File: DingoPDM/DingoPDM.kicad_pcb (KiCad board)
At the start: 4 copper layers, 72.4 x 95.2 mm, 155 parts, among them J1 RedCubeTerminal, J2 RedCubeTerminal, J3 Conn_01x12, J4 TC, J5 USB_C_Receptacle_USB2.0, SW1 BOOT, U1 VXO7805-500-M, U10 BTS7008-2EPA, U11 BTS7008-2EPA, U12 LM324, U13 BTS7008-2EPA, U14 OKI-78SR-5_1.5-W36H-C, U15 TSR_1-2450, U2 LD1117S33CTR, U3 PCA82C250, U4 STM32F446RETx, U5 MB85RC256V, U6 MCP9808, U7 LM324, U8 BTS700n-1EPP, U9 BTS700n-1EPP, Y1 8mHz

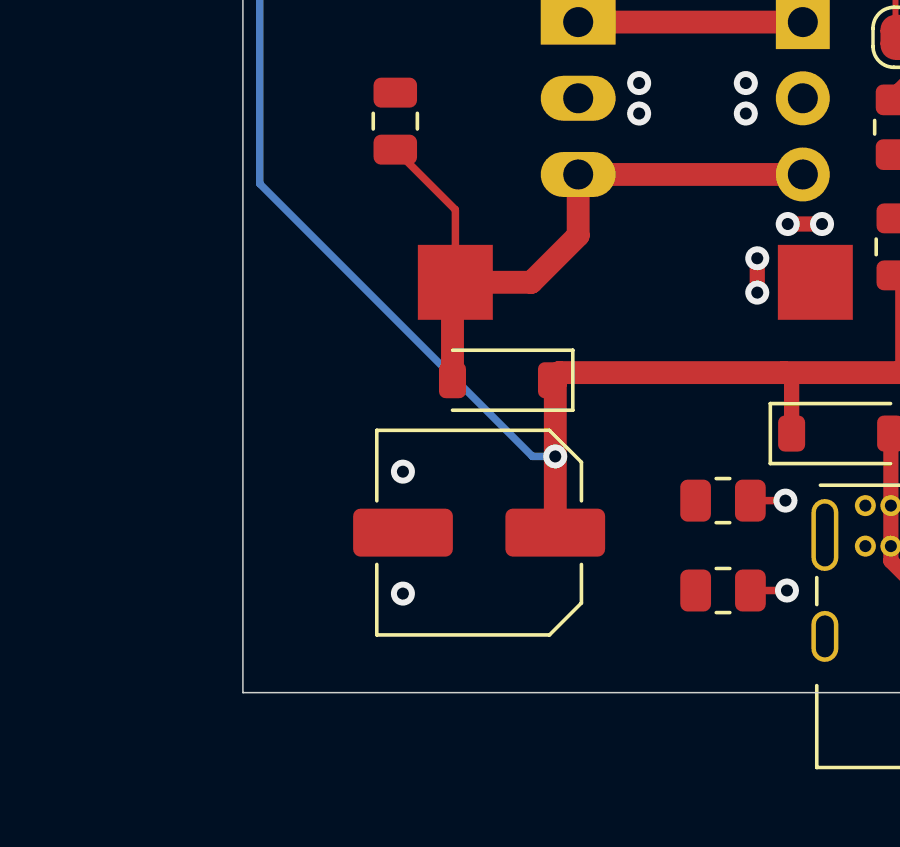
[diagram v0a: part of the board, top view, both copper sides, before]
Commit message: switch to ceramic caps
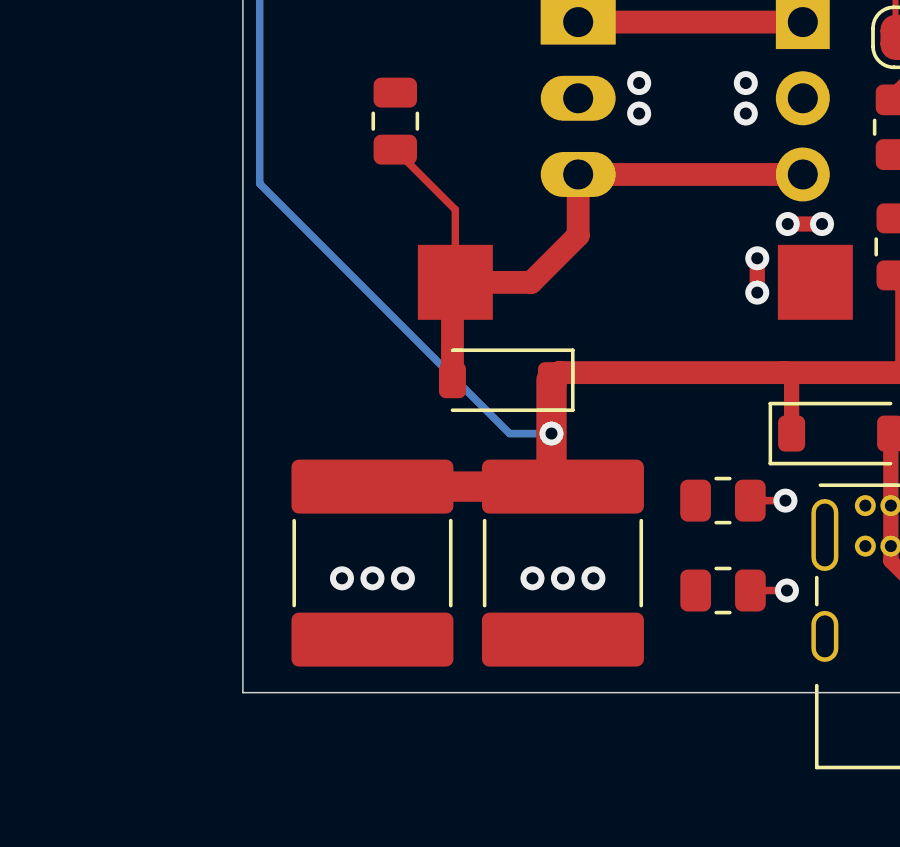
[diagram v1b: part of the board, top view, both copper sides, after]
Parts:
- added C42: 100uF, Capacitor_SMD:C_2220_5750Metric, F.Cu at (-27.2, 57.7)
- C41: footprint Capacitor_SMD:C_Elec_6.3x7.7 -> Capacitor_SMD:C_2220_5750Metric
- moved C41 3.70 mm to (-33.5, 57.7), turned to -90 degrees
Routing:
- net +5V: track 147.2 -> 151.8 mm
- net GND: vias 67 -> 71

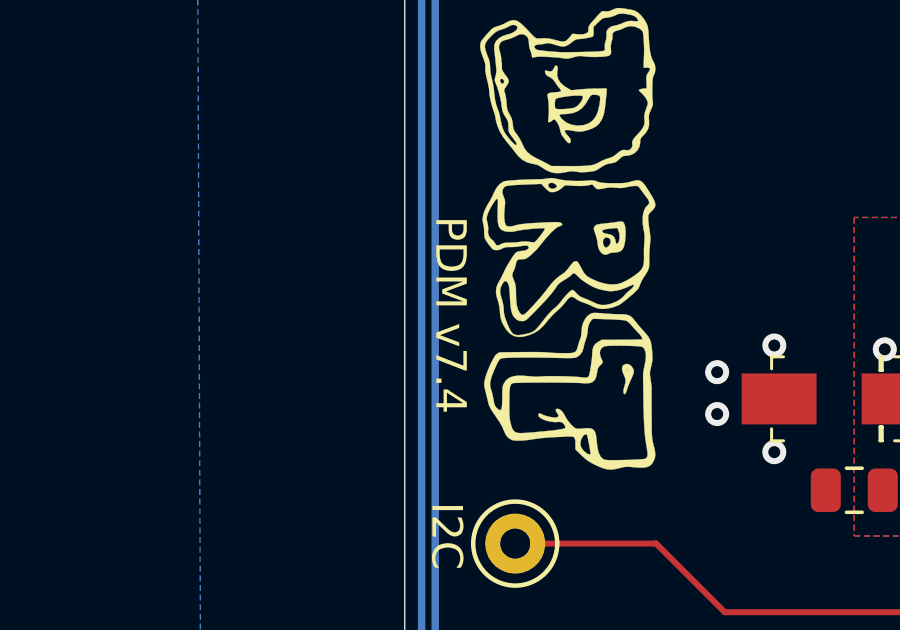
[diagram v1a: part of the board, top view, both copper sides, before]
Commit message: updated silk version
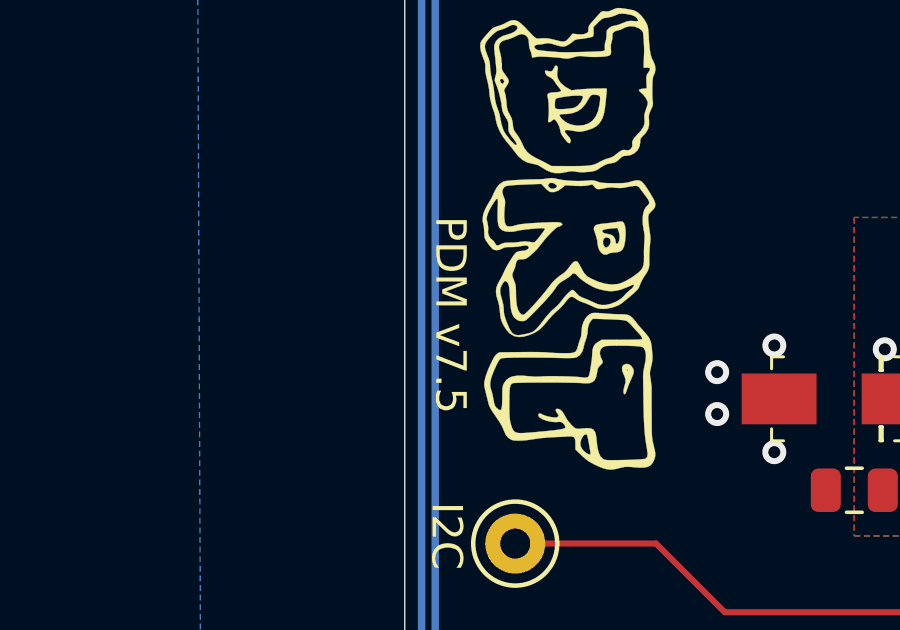
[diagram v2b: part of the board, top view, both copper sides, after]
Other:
- board text added: "PDM v7.5"
- board text removed: "PDM v7.4"
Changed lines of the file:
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@@
 		)
 	)
-	(gr_text "PDM v7.4"
+	(gr_text "PDM v7.5"
 		(at -36.322 3.302 270)
 		(layer "F.SilkS")

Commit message: move footprints to project library
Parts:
- C41, C42: value 100uF -> 47uF
- D10, D8: footprint digikey-footprints:DO-214AC -> dingoPDM:DO-214AC
- D2: footprint digikey-footprints:DO-214AB_TVS -> dingoPDM:DO-214AB_TVS
- D4: footprint digikey-footprints:SOT-23-3 -> dingoPDM:SOT-23-3
- G1: footprint DRTLogo:DRTLogo -> dingoPDM:DRTLogo
- G2: footprint DRTLogo:DingoFaceNoFill -> dingoPDM:DingoFaceNoFill
- J1, J2: footprint RedCube:M6_Hole_8Pin_7461084 -> dingoPDM:M6_Hole_8Pin_7461084
- J3: footprint Deutsch_DT:DT15-12PA -> dingoPDM:DT15-12PA
- SW1: footprint SlideSwitch:CJS-1200TB -> dingoPDM:CJS-1200TB
- U1: footprint CUI_Regulators:VXO78x-500-M -> dingoPDM:VXO78x-500-M
- U10, U11, U13, U8, U9: footprint Profet:TDSO-14 -> dingoPDM:TDSO-14
- U14: footprint Converter_DCDC:Converter_DCDC_Murata_OKI-78SR_Horizontal -> dingoPDM:Converter_DCDC_Murata_OKI-78SR_Horizontal
- U15: footprint Converter_DCDC:Converter_DCDC_TRACO_TSR-1_THT -> dingoPDM:Converter_DCDC_TRACO_TSR-1_THT
- U2: footprint digikey-footprints:SOT-223 -> dingoPDM:SOT-223
- Y1: footprint Crystals_Modify:Crystal_SMD_5032-2Pin_5.0x3.2mm_HandSoldering -> dingoPDM:Crystal_SMD_5032-2Pin_5.0x3.2mm_HandSoldering
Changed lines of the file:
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@@
 		)
 	)
-	(footprint "Crystals_Modify:Crystal_SMD_5032-2Pin_5.0x3.2mm_HandSoldering"
+	(footprint "dingoPDM:Crystal_SMD_5032-2Pin_5.0x3.2mm_HandSoldering"
 		(layer "F.Cu")
 		(at 5.842 55.8546)
@@
 		)
 	)
-	(footprint "RedCube:M6_Hole_8Pin_7461084"
+	(footprint "dingoPDM:M6_Hole_8Pin_7461084"
 		(layer "F.Cu")
 		(at -24.638 27.178)
@@
 		)
 	)
-	(footprint "Profet:TDSO-14"
+	(footprint "dingoPDM:TDSO-14"
 		(layer "F.Cu")
 		(at 11.1448 12.7 90)
@@
 		)
 		(property "Digi-Key_PN" "BTS70021EPPXUMA1CT-ND"
-			(at 23.8448 1.5552 0)
+			(at 1.778 23.622 0)
 			(layer "F.Fab")
 			(hide yes)
@@
 		)
 		(property "LCSC" "C534824"
-			(at 23.8448 1.5552 0)
+			(at 1.778 23.622 0)
 			(layer "F.Fab")
 			(hide yes)
@@
 		)
 	)
-	(footprint "Profet:TDSO-14"
+	(footprint "dingoPDM:TDSO-14"
 		(layer "F.Cu")
 		(at 0.082 12.7 90)
@@
 			)
 		)
-		(property "Digi-Key_PN" "BTS70082EPAXUMA1CT-ND"
-			(at 12.782 12.618 0)
+		(property "Digi-Key_PN" "BTS70021EPPXUMA1CT-ND"
+			(at 1.778 23.622 0)
 			(layer "F.Fab")
 			(hide yes)
@@
 			)
 		)
-		(property "LCSC" "C2150060"
-			(at 12.782 12.618 0)
+		(property "LCSC" "C534824"
+			(at 1.778 23.622 0)
 			(layer "F.Fab")
 			(hide yes)
@@
 		)
 	)
-	(footprint "Deutsch_DT:DT15-12PA"
+	(footprint "dingoPDM:DT15-12PA"
 		(layer "F.Cu")
 		(at 0 0 -90)
@@
 		)
 	)
-	(footprint "CUI_Regulators:VXO78x-500-M"
+	(footprint "dingoPDM:VXO78x-500-M"
 		(layer "F.Cu")
 		(at -24.765 42.799 -90)
@@
 		)
 	)
-	(footprint "digikey-footprints:SOT-23-3"
+	(footprint "dingoPDM:SOT-23-3"
 		(layer "F.Cu")
 		(at -8.8748 -11.2212 -90)
@@
 		)
 	)
-	(footprint "DRTLogo:DRTLogo"
+	(footprint "dingoPDM:DRTLogo"
 		(layer "F.Cu")
 		(at -32.4104 0.762 -90)
@@
 		)
 	)
-	(footprint "digikey-footprints:DO-214AC"
+	(footprint "dingoPDM:DO-214AC"
 		(layer "F.Cu")
 		(at -23.368 6.096 180)
@@
 		)
 	)
-	(footprint "Profet:TDSO-14"
+	(footprint "dingoPDM:TDSO-14"
 		(layer "F.Cu")
 		(at 8.9604 -12.5528 -90)
 		(descr "Original name <b>SOP65P600X115-15N-V</b><p>Max Component Height - 1.15mm")
 		(property "Reference" "U10"
-			(at 0.73 -4.07 90)
+			(at 0.73 -4.07 270)
 			(layer "F.SilkS")
 			(hide yes)
@@
 		)
 		(property "Value" "BTS7008-2EPA"
-			(at 14.974 4.124 90)
+			(at 14.974 4.124 270)
 			(layer "F.Fab")
 			(hide yes)
@@
 			)
 		)
-		(property "Digi-Key_PN" "BTS70082EPAXUMA1CT-ND"
-			(at 21.5132 -3.5924 0)
+		(property "Digi-Key_PN" "BTS70021EPPXUMA1CT-ND"
+			(at 1.778 23.622 180)
 			(layer "F.Fab")
 			(hide yes)
@@
 			)
 		)
-		(property "LCSC" "C2150060"
-			(at 21.5132 -3.5924 0)
+		(property "LCSC" "C534824"
+			(at 1.778 23.622 180)
 			(layer "F.Fab")
 			(hide yes)
@@
 		)
 	)
-	(footprint "Profet:TDSO-14"
+	(footprint "dingoPDM:TDSO-14"
 		(layer "F.Cu")
 		(at 0.0104 -12.6544 -90)
 		(descr "Original name <b>SOP65P600X115-15N-V</b><p>Max Component Height - 1.15mm")
 		(property "Reference" "U13"
-			(at 0.73 -4.07 90)
+			(at 0.73 -4.07 270)
 			(layer "F.SilkS")
 			(hide yes)
@@
 		)
 		(property "Value" "BTS7008-2EPA"
-			(at 14.974 4.124 90)
+			(at 14.974 4.124 270)
 			(layer "F.Fab")
 			(hide yes)
@@
 			)
 		)
-		(property "Digi-Key_PN" "BTS70082EPAXUMA1CT-ND"
-			(at 12.6648 -12.644 0)
+		(property "Digi-Key_PN" "BTS70021EPPXUMA1CT-ND"
+			(at 1.778 23.622 180)
 			(layer "F.Fab")
 			(hide yes)
@@
 			)
 		)
-		(property "LCSC" "C2150060"
-			(at 12.6648 -12.644 0)
+		(property "LCSC" "C534824"
+			(at 1.778 23.622 180)
 			(layer "F.Fab")
 			(hide yes)
@@
 		)
 	)
-	(footprint "Converter_DCDC:Converter_DCDC_TRACO_TSR-1_THT"
+	(footprint "dingoPDM:Converter_DCDC_TRACO_TSR-1_THT"
 		(layer "F.Cu")
 		(at -26.67 39.624 -90)
@@
 		)
 	)
-	(footprint "digikey-footprints:DO-214AC"
+	(footprint "dingoPDM:DO-214AC"
 		(layer "F.Cu")
 		(at 22.86 6.096)
 		(property "Reference" "D8"
-			(at 0 -2.6 0)
+			(at 0 -2.6 180)
 			(layer "F.SilkS")
 			(hide yes)
@@
 		)
 		(property "Value" "BYG23M"
-			(at 0 2.45 0)
+			(at 0 2.45 180)
 			(layer "F.Fab")
 			(hide yes)
@@
 		)
 		(property "Digi-Key_PN" "BYG23M-E3/TR3GICT-ND"
-			(at 0 0 0)
+			(at -46.736 12.192 180)
 			(layer "F.Fab")
 			(hide yes)
@@
 		)
 		(property "LCSC" "C141573"
-			(at 0 0 0)
+			(at -46.736 12.192 180)
 			(layer "F.Fab")
 			(hide yes)
@@
 		)
 	)
-	(footprint "digikey-footprints:SOT-223"
+	(footprint "dingoPDM:SOT-223"
 		(layer "F.Cu")
 		(at -11.3386 44.094)
@@
 		)
 	)
-	(footprint "Converter_DCDC:Converter_DCDC_Murata_OKI-78SR_Horizontal"
+	(footprint "dingoPDM:Converter_DCDC_Murata_OKI-78SR_Horizontal"
 		(layer "F.Cu")
 		(at -19.182 39.624 -90)
@@
 		(embedded_fonts no)
 	)
-	(footprint "Profet:TDSO-14"
+	(footprint "dingoPDM:TDSO-14"
 		(layer "F.Cu")
 		(at -10.922 12.7 90)
@@
 		)
 	)
-	(footprint "digikey-footprints:DO-214AB_TVS"
+	(footprint "dingoPDM:DO-214AB_TVS"
 		(layer "F.Cu")
 		(at -33.655 30.586 -90)
@@
 		)
 	)
-	(footprint "SlideSwitch:CJS-1200TB"
+	(footprint "dingoPDM:CJS-1200TB"
 		(layer "F.Cu")
 		(at -5.461 58.166 90)
@@
 			)
 		)
-		(property "Value" "100uF"
+		(property "Value" "47uF"
 			(at 0 3.65 270)
 			(layer "F.Fab")
@@
 			)
 		)
-		(property "Value" "100uF"
+		(property "Value" "47uF"
 			(at 0 3.65 270)
 			(layer "F.Fab")
@@
 		)
 	)
-	(footprint "RedCube:M6_Hole_8Pin_7461084"
+	(footprint "dingoPDM:M6_Hole_8Pin_7461084"
 		(layer "F.Cu")
 		(at -30.48 -27.178)
@@
 		)
 	)
-	(footprint "DRTLogo:DingoFaceNoFill"
+	(footprint "dingoPDM:DingoFaceNoFill"
 		(layer "B.Cu")
 		(at -25.781 -7.493 180)
@@
 		)
 		(property "Datasheet" ""
-			(at 0 0 180)
+			(at 0 0 0)
 			(layer "F.Fab")
 			(hide yes)
@@
 		)
 		(property "Description" ""
-			(at 0 0 180)
+			(at 0 0 0)
 			(layer "F.Fab")
 			(hide yes)

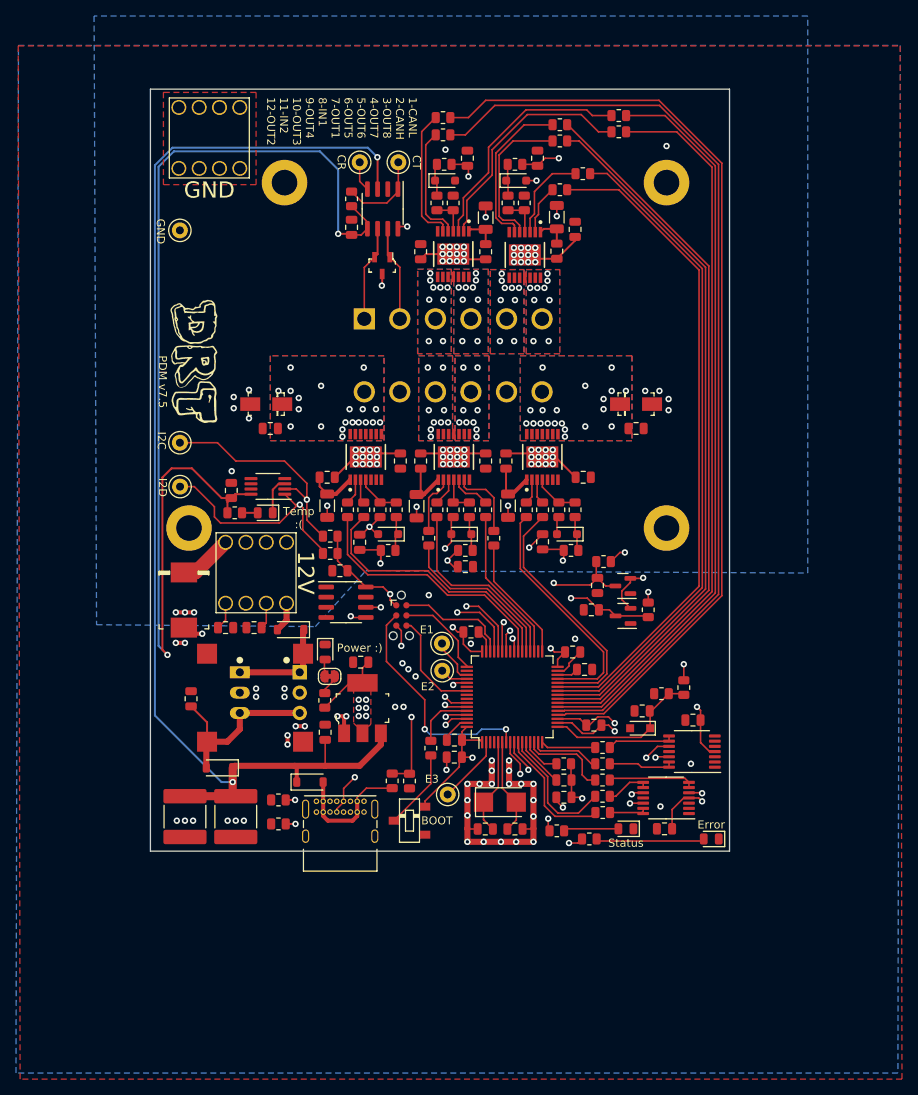
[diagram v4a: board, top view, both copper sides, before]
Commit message: make v7.6 changes, update can transceiver
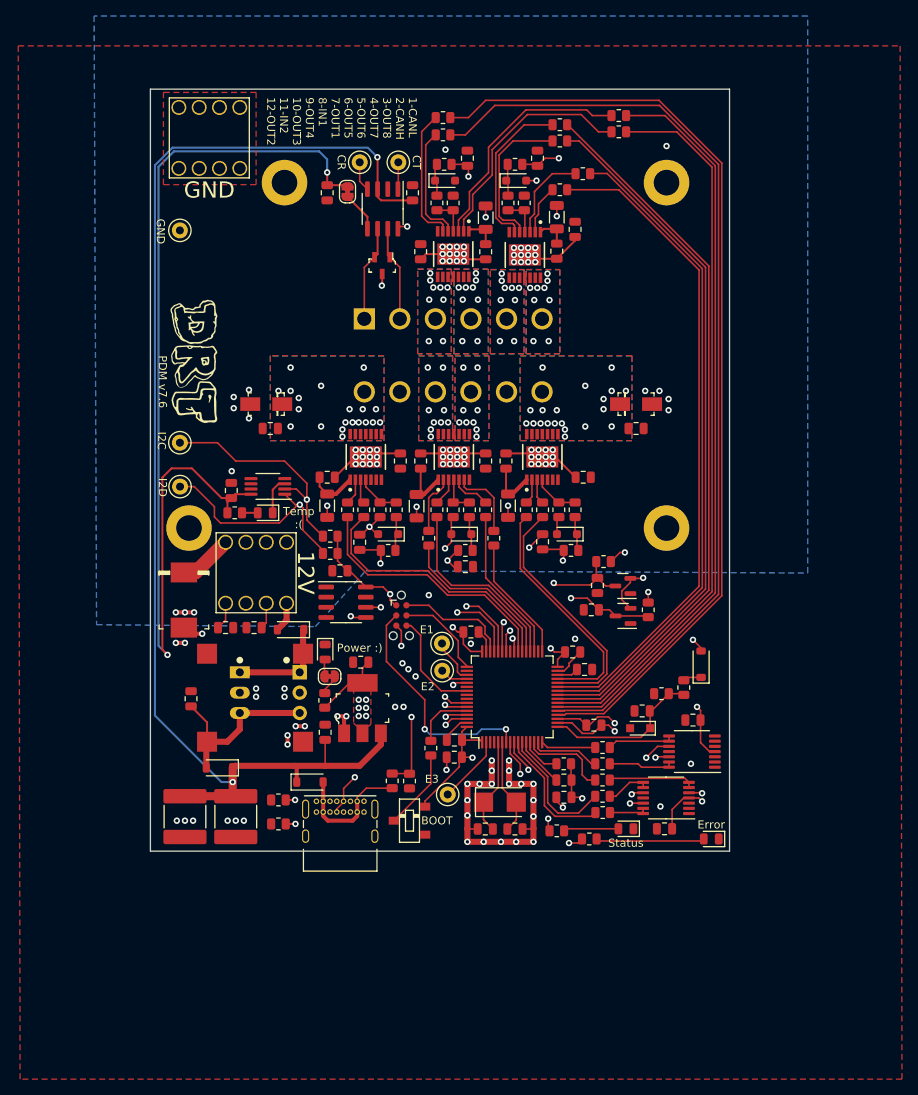
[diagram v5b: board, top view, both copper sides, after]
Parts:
- removed R5: 1K, Resistor_SMD:R_0805_2012Metric
- added C43: 100nF, Capacitor_SMD:C_0805_2012Metric, F.Cu at (-5.08, -20.3)
- added D20: Schottky, Diode_SMD:D_SOD-123, F.Cu at (31.0, 38.6)
- added JP2: VioJumper, Jumper:SolderJumper-2_P1.3mm_Bridged_RoundedPad1.0x1.5mm, F.Cu at (-13.2, -20.5)
- U3: value PCA82C250 -> TJA1042T/3
- moved C9 5.29 mm to (-15.7, -20.3), turned to -90 degrees
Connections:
- R1 pad 1: +12V -> Net-(D20-K)
- U3 pad 5: +3V3 -> Net-(JP2-B)
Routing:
- net +3V3: track 221.3 -> 209.5 mm
- net /MCU/CAN_TX: track 113.0 -> 105.7 mm
- net +5V: track 151.8 -> 157.4 mm
- net Net-(JP2-B): track 0.00 -> 5.02 mm
- net +12V: track 97.3 -> 94.5 mm
- net Net-(D20-K): track 0.00 -> 2.31 mm
- removed copper zone on B.Cu, net +3V3
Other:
- board text added: "PDM v7.6"
- board text removed: "PDM v7.5"

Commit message: fix 3.3v plane that disappeared
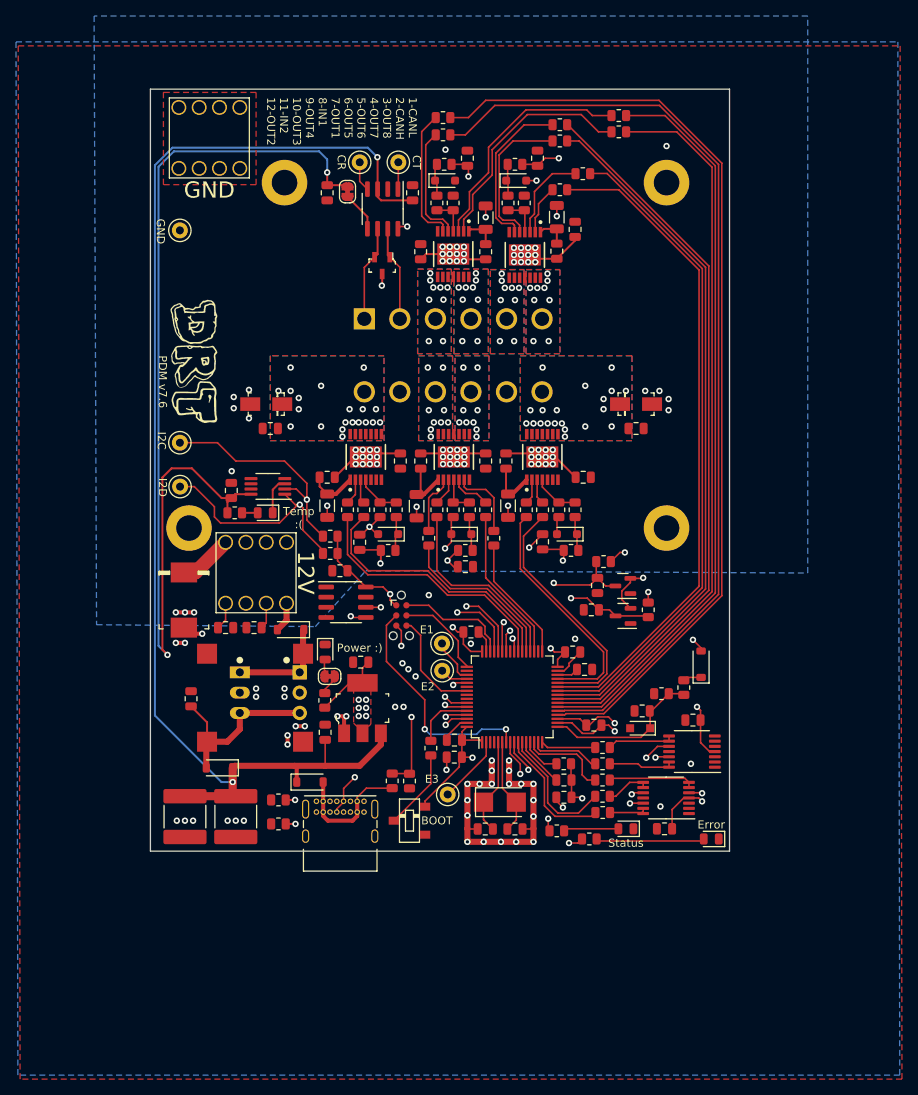
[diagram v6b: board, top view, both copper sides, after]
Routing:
- added copper zone on B.Cu, net +3V3
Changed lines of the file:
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@@
+	)
+	(zone
+		(net 20)
+		(net_name "+3V3")
+		(layer "B.Cu")
+		(hatch edge 0.5)
+		(connect_pads
+			(clearance 0.254)
+		)
+		(min_thickness 0.2032)
+		(filled_areas_thickness no)
+		(fill yes
+			(thermal_gap 0.508)
+			(thermal_bridge_width 0.508)
+			(smoothing fillet)
+			(radius 0.508)
+		)
+		(polygon
+			(pts
+				(xy -54.64746 -39.183249) (xy 55.58854 -39.183249) (xy 55.820423 89.975751) (xy -54.415577 89.975751)
+			)
+		)
 	)
 	(zone
